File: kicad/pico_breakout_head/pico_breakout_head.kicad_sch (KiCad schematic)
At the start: 16 parts, among them J1 Conn_01x03, J2 JST PH 5-pin male thru vertic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, J3 Conn_01x03, J34 Conn_01x03, J4 Conn_01x03, J5 XH2.54

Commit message: ESP32 breakout v1.0
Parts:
- removed J1, J3, J34, J4: Conn_01x03, symbol Connector_Generic:Conn_01x03
- removed J2: JST PH 5-pin male thru vertical, Connector_JST:JST_PH_B5B-PH-K_1x05_P2.00mm_Vertical, symbol Connector_Generic:Conn_01x05
- removed R6: 0, symbol Device:R_Small_US
- removed R7, R8, R9: 1k, symbol Device:R_Small_US
- removed U2: ~, symbol Kaia_v2:RASPBERRY-PI-PICO
- added D1: CGRA4004-G, Diode_SMD:D_SMA, symbol Device:D
- added H1, H2, H3, H4: MountingHole, MountingHole:MountingHole_3.2mm_M3, symbol Mechanical:MountingHole
- added J1, J2: HDR F 2.54MM 20-pin VERT, Connector_PinHeader_2.54mm:PinHeader_1x20_P2.54mm_Vertical, symbol Connector_Generic:Conn_01x20
- added J3: JST B6B-PH-K-S, Connector_JST:JST_PH_B6B-PH-K_1x06_P2.00mm_Vertical, symbol Connector_Generic:Conn_01x06
- added J4: HDR M 2.54MM 4p VERT, Connector_PinHeader_2.54mm:PinHeader_1x04_P2.54mm_Vertical, symbol Connector_Generic:Conn_01x04
- added J6: HDR M 2.54MM 9p VERT, Connector_PinHeader_2.54mm:PinHeader_1x09_P2.54mm_Vertical, symbol Connector_Generic:Conn_01x09
- added Q1: BSS123, Package_TO_SOT_SMD:SOT-23, symbol Transistor_FET:BSS123
- added U1: Pico, Makerspet:RPi_Pico_SMD_TH, symbol Makerspet:Pico
- J5: value XH2.54 -> JST B2B-XH-A
- R1, R2, R3: value 10M -> 1M; footprint (none) -> Resistor_SMD:R_0603_1608Metric
- R4: value 0 -> 1M; footprint (none) -> Resistor_SMD:R_0603_1608Metric
- R5: value 0 -> 1k; footprint (none) -> Resistor_SMD:R_0603_1608Metric
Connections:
- net TOUCH_CTL is gone; now on net +5V: R1.2, R2.2, R3.2
- net +3.3V: now also J2.5 (Pin_5), U1.36 (3V3)
- net +5V: now also J5.1 (Pin_1), R4.2, D1.1 (K), J1.13 (Pin_13), J1.18 (Pin_18), J1.3 (Pin_3), J1.8 (Pin_8), J2.13 (Pin_13), J2.18 (Pin_18), J2.3 (Pin_3), J2.8 (Pin_8), J3.1 (Pin_1), J3.6 (Pin_6), J6.1 (Pin_1), J6.2 (Pin_2), J6.4 (Pin_4), J6.5 (Pin_5), J6.7 (Pin_7), J6.8 (Pin_8), Q1.3 (D), U1.13 (GND), U1.18 (GND), U1.23 (GND), U1.28 (GND), U1.3 (GND), U1.33 (AGND), U1.38 (GND), U1.8 (GND)
- net SERVO_LEFT: now also J1.5 (Pin_5), J6.3 (Pin_3), U1.5 (GPIO3)
- net SERVO_RIGHT: now also J1.6 (Pin_6), J6.6 (Pin_6), U1.6 (GPIO4)
- net TOUCH_RIGHT: now reaches R3.1
- net TOUCH_RIGHT: now also J1.11 (Pin_11), J4.3 (Pin_3), U1.11 (GPIO8)
- net FAN_EN: now reaches R5.2
- net FAN_EN: now also J1.14 (Pin_14), U1.14 (GPIO10); no longer R2.1
- net at J5.2 (Pin_2): now also D1.2 (A), Q1.2 (S)
- net at R5.1: now also Q1.1 (G)
- net TOUCH_REAR: now reaches R4.1
- net TOUCH_REAR: now also J1.12 (Pin_12), J4.4 (Pin_4), U1.12 (GPIO9)
- net TOUCH_TOP: now reaches R1.1
- net TOUCH_TOP: now also J1.9 (Pin_9), J4.1 (Pin_1), U1.9 (GPIO6); no longer R4.2
- new net: J2.1 (Pin_1), U1.40 (VBUS)
- new net: J2.10 (Pin_10), U1.31 (GPIO26_ADC0)
- new net: J2.11 (Pin_11), U1.30 (RUN)
- new net: J2.12 (Pin_12), U1.29 (GPIO22)
- new net: J2.14 (Pin_14), U1.27 (GPIO21)
- new net: J2.15 (Pin_15), U1.26 (GPIO20)
- new net: J2.16 (Pin_16), U1.25 (GPIO19)
- new net: J2.17 (Pin_17), U1.24 (GPIO18)
- new net: J2.19 (Pin_19), U1.22 (GPIO17)
- new net: J2.2 (Pin_2), U1.39 (VSYS)
- new net: J2.20 (Pin_20), U1.21 (GPIO16)
- new net: J2.4 (Pin_4), U1.37 (3V3_EN)
- new net: J2.6 (Pin_6), U1.35 (ADC_VREF)
- new net: J2.7 (Pin_7), U1.34 (GPIO28_ADC2)
- new net: J2.9 (Pin_9), U1.32 (GPIO27_ADC1)
- new net: J1.15 (Pin_15), U1.15 (GPIO11)
- new net: J1.16 (Pin_16), U1.16 (GPIO12)
- new net: J1.17 (Pin_17), U1.17 (GPIO13)
- new net: J1.19 (Pin_19), U1.19 (GPIO14)
- new net: J1.20 (Pin_20), U1.20 (GPIO15)
- new net I2C_SCL_MASTER: J1.2 (Pin_2), J3.3 (Pin_3), U1.2 (GPIO1)
- new net I2C_SDA_MASTER: J1.1 (Pin_1), J3.4 (Pin_4), U1.1 (GPIO0)
- new net INT_MASTER: J1.4 (Pin_4), J3.5 (Pin_5), U1.4 (GPIO2)
- new net SERVO_EXT: J1.7 (Pin_7), J6.9 (Pin_9), U1.7 (GPIO5)
- new net TOUCH_LEFT: J1.10 (Pin_10), J4.2 (Pin_2), R2.1, U1.10 (GPIO7)
- no-connect marks 5 -> 4
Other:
- note added: "FAN 5V 40x40mm 2-pin"
- note added: "I2C MASTER"
- note added: "SERVOS 5V MG90S"
- note added: "TOUCH Sticky copper tape"
- note removed: "2.54mm header"
- note removed: "FAN"
- note removed: "TODO - mic array"
- note removed: "Touch"
- moved on the sheet: R1, R2, R3

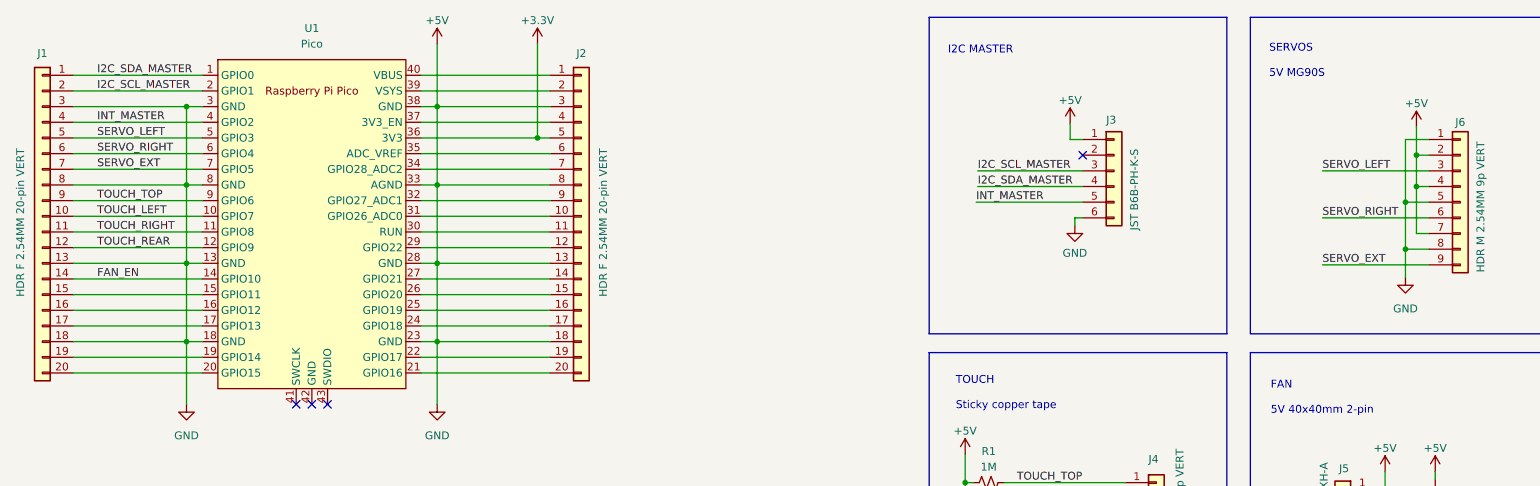
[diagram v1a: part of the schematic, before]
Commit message: Raspberry Pi Pico head extension PCB proto
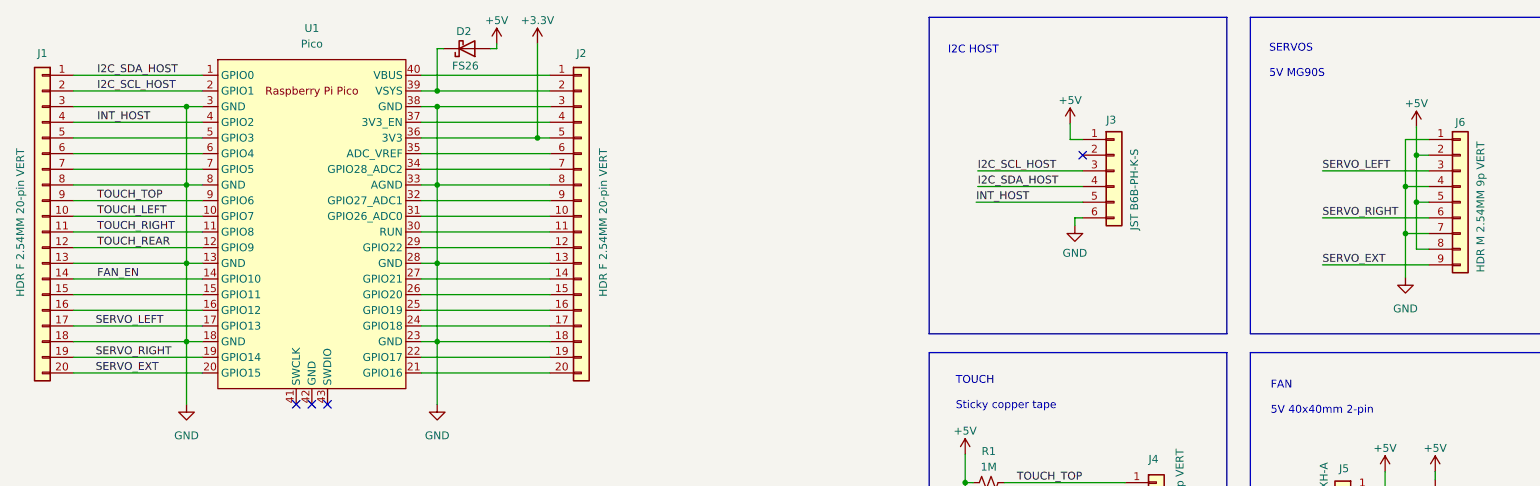
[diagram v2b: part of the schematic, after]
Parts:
- added D2: FS26, Diode_SMD:D_SOD-123F, symbol Device:D_Schottky
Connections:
- net +5V: now also D2.2 (A); no longer J1.13 (Pin_13), J1.18 (Pin_18), J1.3 (Pin_3), J1.8 (Pin_8), J2.13 (Pin_13), J2.18 (Pin_18), J2.3 (Pin_3), J2.8 (Pin_8), J3.6 (Pin_6), J6.1 (Pin_1), J6.4 (Pin_4), J6.7 (Pin_7), Q1.3 (D), U1.13 (GND), U1.18 (GND), U1.23 (GND), U1.28 (GND), U1.3 (GND), U1.33 (AGND), U1.38 (GND), U1.8 (GND)
- net SERVO_EXT: now also J1.20 (Pin_20), U1.20 (GPIO15); no longer J1.7 (Pin_7), U1.7 (GPIO5)
- net SERVO_LEFT: now also J1.17 (Pin_17), U1.17 (GPIO13); no longer J1.5 (Pin_5), U1.5 (GPIO3)
- net SERVO_RIGHT: now also J1.19 (Pin_19), U1.19 (GPIO14); no longer J1.6 (Pin_6), U1.6 (GPIO4)
- net at J2.2 (Pin_2), U1.39 (VSYS): now also D2.1 (K)
- net I2C_SCL_MASTER renamed I2C_SCL_HOST
- net I2C_SDA_MASTER renamed I2C_SDA_HOST
- net INT_MASTER renamed INT_HOST
- new net: J1.5 (Pin_5), U1.5 (GPIO3)
- new net: J1.6 (Pin_6), U1.6 (GPIO4)
- new net: J1.7 (Pin_7), U1.7 (GPIO5)
- new net GND: J1.13 (Pin_13), J1.18 (Pin_18), J1.3 (Pin_3), J1.8 (Pin_8), J2.13 (Pin_13), J2.18 (Pin_18), J2.3 (Pin_3), J2.8 (Pin_8), J3.6 (Pin_6), J6.1 (Pin_1), J6.4 (Pin_4), J6.7 (Pin_7), Q1.3 (D), U1.13 (GND), U1.18 (GND), U1.23 (GND), U1.28 (GND), U1.3 (GND), U1.33 (AGND), U1.38 (GND), U1.8 (GND)
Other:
- note added: "I2C HOST"
- note removed: "I2C MASTER"

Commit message: Socket header
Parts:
- J1, J2: footprint Connector_PinHeader_2.54mm:PinHeader_1x20_P2.54mm_Vertical -> Connector_PinSocket_2.54mm:PinSocket_1x20_P2.54mm_Vertical
- J4: footprint Connector_PinHeader_2.54mm:PinHeader_1x04_P2.54mm_Vertical -> Connector_PinSocket_2.54mm:PinSocket_1x04_P2.54mm_Vertical
- J6: footprint Connector_PinHeader_2.54mm:PinHeader_1x09_P2.54mm_Vertical -> Connector_PinSocket_2.54mm:PinSocket_1x09_P2.54mm_Vertical
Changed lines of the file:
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@@
       (effects (font (size 1.27 1.27)))
     )
-    (property "Footprint" "Connector_PinHeader_2.54mm:PinHeader_1x20_P2.54mm_Vertical" (at 107.696 48.006 0)
+    (property "Footprint" "Connector_PinSocket_2.54mm:PinSocket_1x20_P2.54mm_Vertical" (at 107.696 48.006 0)
       (effects (font (size 1.27 1.27)) hide)
     )
@@
       (effects (font (size 1.27 1.27)) (justify left))
     )
-    (property "Footprint" "Connector_PinHeader_2.54mm:PinHeader_1x04_P2.54mm_Vertical" (at 200.914 93.726 0)
+    (property "Footprint" "Connector_PinSocket_2.54mm:PinSocket_1x04_P2.54mm_Vertical" (at 200.914 93.726 0)
       (effects (font (size 1.27 1.27)) hide)
     )
@@
       (effects (font (size 1.27 1.27)))
     )
-    (property "Footprint" "Connector_PinHeader_2.54mm:PinHeader_1x20_P2.54mm_Vertical" (at 20.32 48.006 0)
+    (property "Footprint" "Connector_PinSocket_2.54mm:PinSocket_1x20_P2.54mm_Vertical" (at 20.32 48.006 0)
       (effects (font (size 1.27 1.27)) hide)
     )
@@
       (effects (font (size 1.27 1.27)))
     )
-    (property "Footprint" "Connector_PinHeader_2.54mm:PinHeader_1x09_P2.54mm_Vertical" (at 250.19 45.72 0)
-      (effects (font (size 1.27 1.27)) hide)
-    )
+    (property "Footprint" "Connector_PinSocket_2.54mm:PinSocket_1x09_P2.54mm_Vertical" (at 250.19 45.72 0)
+      (effects (font (size 1.27 1.27)) hide)
+    )

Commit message: Pico head PCB 0.1.1
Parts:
- removed D1: CGRA4004-G, Diode_SMD:D_SMA, symbol Device:D
- removed R5: 1k, Resistor_SMD:R_0603_1608Metric, symbol Device:R_Small_US
- added D1: FS26, Diode_SMD:D_SOD-123F, symbol Device:D_Schottky
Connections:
- net +5V: now also D1.1 (K)
- net FAN_EN: now also Q1.1 (G)
- net at J5.2 (Pin_2), Q1.2 (S): now also D1.2 (A)
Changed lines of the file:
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@@
   (title_block
     (title "Raspberry Pi Pico Breakout - Head")
+    (date "2023-12-21")
+    (rev "0.1.1")
     (company "Maker's Pet")
     (comment 1 "makerspet.com")
@@
     (stroke (width 0) (type default))
   )
+  (wire (pts (xy 223.774 104.648) (xy 238.506 104.648))
+    (stroke (width 0) (type default))
+  )
   (wire (pts (xy 81.788 40.386) (xy 102.616 40.386))
     (stroke (width 0) (type default))
@@
     (stroke (width 0) (type default))
   )
-  (wire (pts (xy 223.774 104.648) (xy 231.521 104.648))
-    (stroke (width 0) (type default))
-  )
   (wire (pts (xy 25.4 45.466) (xy 46.228 45.466))
     (stroke (width 0) (type default))
@@
   )
   (wire (pts (xy 81.788 25.146) (xy 102.616 25.146))
-    (stroke (width 0) (type default))
-  )
-  (wire (pts (xy 236.601 104.648) (xy 238.506 104.648))
     (stroke (width 0) (type default))
   )
@@
     )
   )
-  (symbol (lib_id "Device:R_Small_US") (at 234.061 104.648 270) (unit 1)
-    (in_bom yes) (on_board yes) (dnp no) (fields_autoplaced)
-    (property "Reference" "R5" (at 234.061 99.568 90)
-      (effects (font (size 1.27 1.27)))
-    )
-    (property "Value" "1k" (at 234.061 102.108 90)
-      (effects (font (size 1.27 1.27)))
-    )
-    (property "Footprint" "Resistor_SMD:R_0603_1608Metric" (at 234.061 104.648 0)
-      (effects (font (size 1.27 1.27)) hide)
-    )
-    (property "Datasheet" "~" (at 234.061 104.648 0)
-      (effects (font (size 1.27 1.27)) hide)
-    )
-    (pin "1")
-    (pin "2")
-    (instances
-      (project "pico_breakout_head"
-        (path "/e24ae185-8f18-408c-aee8-f727519bade3"
-          (reference "R5") (unit 1)
-        )
-      )
-    )
-  )
   (symbol (lib_id "power:GND") (at 84.328 78.486 0) (unit 1)
     (in_bom yes) (on_board yes) (dnp no) (fields_autoplaced)
@@
     )
   )
-  (symbol (lib_id "Device:D") (at 246.126 94.488 270) (unit 1)
-    (in_bom yes) (on_board yes) (dnp no) (fields_autoplaced)
-    (property "Reference" "D1" (at 248.666 93.218 90)
-      (effects (font (size 1.27 1.27)) (justify left))
-    )
-    (property "Value" "CGRA4004-G" (at 248.666 95.758 90)
-      (effects (font (size 1.27 1.27)) (justify left))
-    )
-    (property "Footprint" "Diode_SMD:D_SMA" (at 246.126 94.488 0)
-      (effects (font (size 1.27 1.27)) hide)
-    )
-    (property "Datasheet" "~" (at 246.126 94.488 0)
-      (effects (font (size 1.27 1.27)) hide)
-    )
-    (property "Sim.Device" "D" (at 246.126 94.488 0)
-      (effects (font (size 1.27 1.27)) hide)
-    )
-    (property "Sim.Pins" "1=K 2=A" (at 246.126 94.488 0)
-      (effects (font (size 1.27 1.27)) hide)
-    )
-    (pin "1")
-    (pin "2")
-    (instances
-      (project "pico_breakout_head"
-        (path "/e24ae185-8f18-408c-aee8-f727519bade3"
-          (reference "D1") (unit 1)
-        )
-      )
-    )
-  )
   (symbol (lib_id "Mechanical:MountingHole") (at 137.7029 197.6235 0) (unit 1)
     (in_bom yes) (on_board yes) (dnp no) (fields_autoplaced)
@@
         )
       )
+    )
+  )
+  (symbol (lib_id "Device:D_Schottky") (at 246.126 94.488 90) (mirror x) (unit 1)
+    (in_bom yes) (on_board yes) (dnp no)
+    (property "Reference" "D1" (at 248.92 93.98 0)
+      (effects (font (size 1.27 1.27)))
+    )
+    (property "Value" "FS26" (at 243.332 94.234 0)
+      (effects (font (size 1.27 1.27)))
+    )
+    (property "Footprint" "Diode_SMD:D_SOD-123F" (at 246.126 94.488 0)
+      (effects (font (size 1.27 1.27)) hide)
+    )
+    (property "Datasheet" "https://www.digikey.com/en/products/detail/good-ark-semiconductor/FS26/18667798" (at 246.126 94.488 0)
+      (effects (font (size 1.27 1.27)) hide)
+    )
+    (pin "2")
+    (pin "1")
+    (instances
+      (project "pico_breakout_head"
+        (path "/e24ae185-8f18-408c-aee8-f727519bade3"
+          (reference "D1") (unit 1)
+        )
+      )

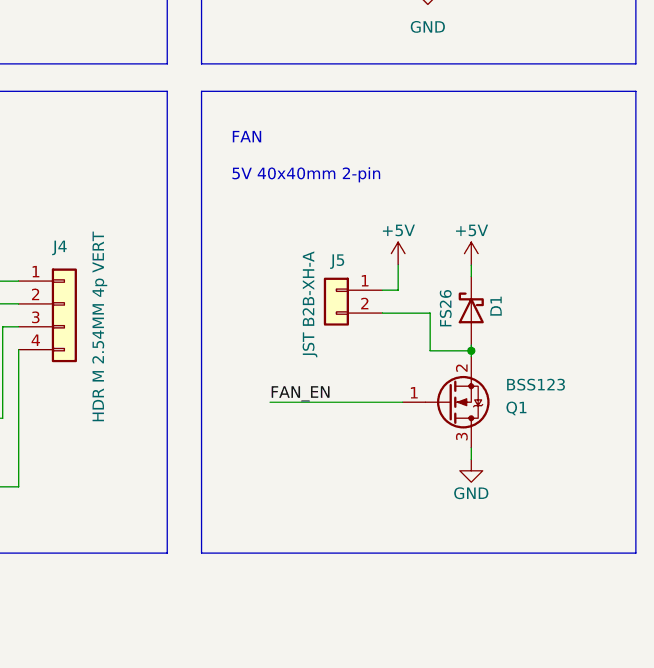
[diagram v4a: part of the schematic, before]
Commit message: Alt fuse; fan fix
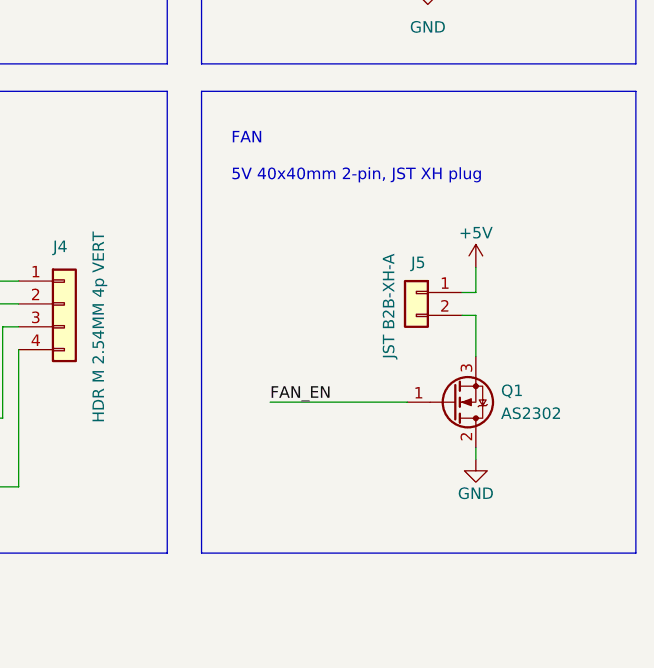
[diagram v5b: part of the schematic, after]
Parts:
- removed D1: FS26, Diode_SMD:D_SOD-123F, symbol Device:D_Schottky
- removed Q1: BSS123, Package_TO_SOT_SMD:SOT-23, symbol Transistor_FET:BSS123
- added Q1: AS2302, Package_TO_SOT_SMD:SOT-23, symbol Makerspet:AS2302
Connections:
- net FAN_EN: now also Q1.1 (G)
- net GND: now also Q1.2 (D)
- net at J5.2 (Pin_2): now also Q1.3 (S)
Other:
- note added: "FAN 5V 40x40mm 2-pin, JST XH plug"
- note removed: "FAN 5V 40x40mm 2-pin"
- moved on the sheet: J5
